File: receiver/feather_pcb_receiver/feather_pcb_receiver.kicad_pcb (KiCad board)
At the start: 2 copper layers, 15 parts, among them J2 uC_Flash, J3 VESC Conn, J4 Utilities Conn, U1 AP2112K-3.3, U2 ATSAMD21G18A-AUT, U3 nRF24L01+, Y1 ABS06-127-32.768KHZ-T‎

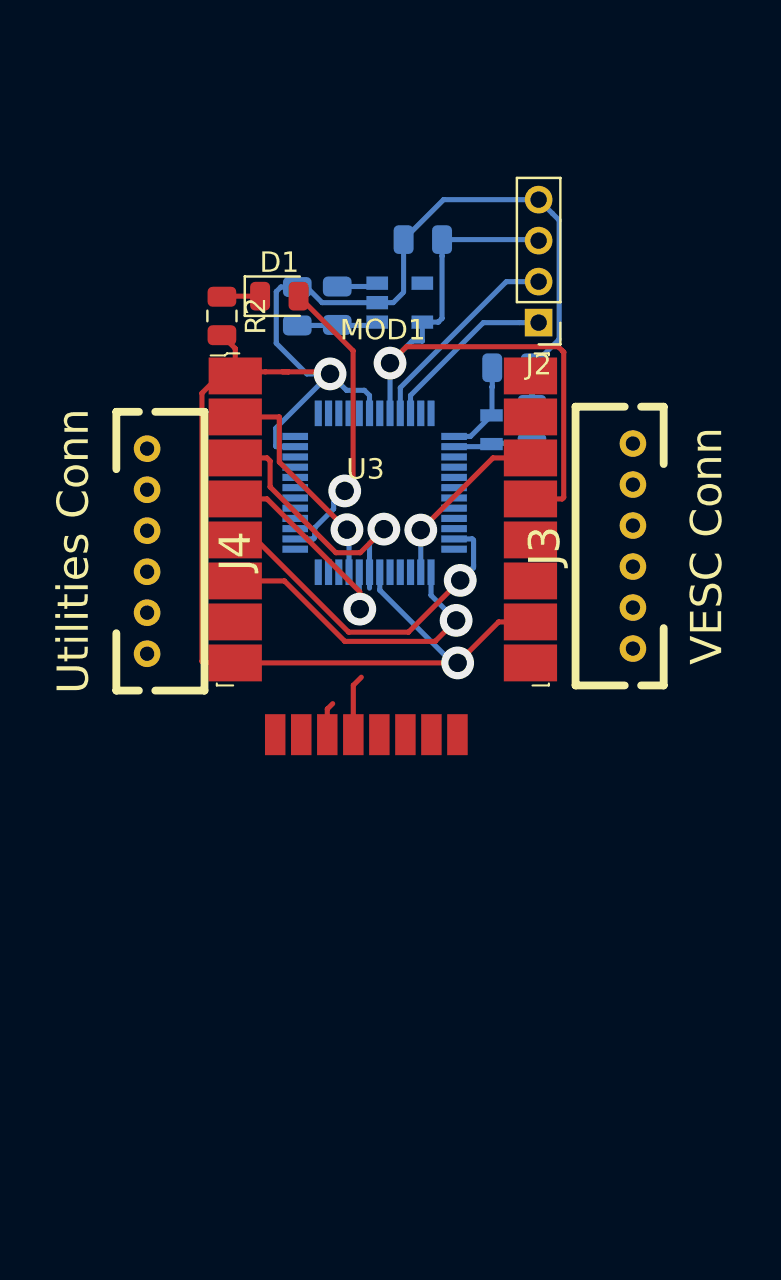
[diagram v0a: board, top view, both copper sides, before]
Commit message: rfm module layout
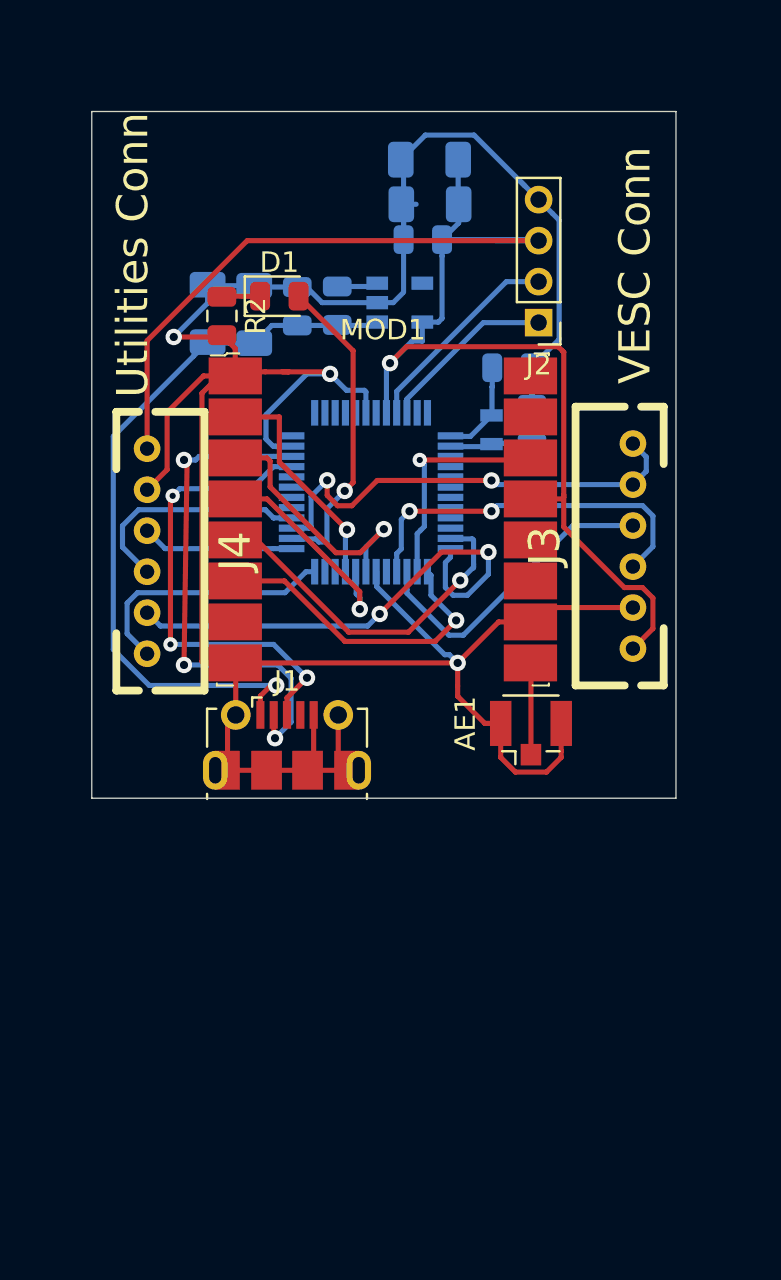
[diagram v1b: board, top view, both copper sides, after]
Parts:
- removed U3: nRF24L01+, mysensors_radios:NRF24L01_PA_LNA-SMD
- added AE1: Antenna_Shield, Connector_Coaxial:U.FL_Hirose_U.FL-R-SMT-1_Vertical, F.Cu at (116.4, 72.3)
- added C1: CP_Small, Capacitor_SMD:C_1206_3216Metric, B.Cu at (102.9, 51.9)
- added C2: 10uF, Capacitor_SMD:C_1206_3216Metric, B.Cu at (100.7, 51.9)
- added C5: 10uF, Capacitor_SMD:C_1206_3216Metric, B.Cu at (111.5, 46.5)
- added C6: CP_Small, Capacitor_SMD:C_1206_3216Metric, B.Cu at (111.5, 44.4)
- added J1: USB_B_Micro, Connector_USB:USB_Micro-B_Molex-105017-0001, F.Cu at (104.5, 72.9)
- moved U2 0.18 mm to (108.6, 60.6)
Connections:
- J3 pad 1: (no net) -> +3V3
- J3 pad 2: (no net) -> GND
- J3 pad 3: (no net) -> VESC1
- J3 pad 4: (no net) -> VESC2
- J3 pad 5: (no net) -> VESC3
- J3 pad 6: (no net) -> VESC3
- J4 pad 1: (no net) -> +3V3
- J4 pad 2: (no net) -> GND
- J4 pad 3: (no net) -> UT1
- J4 pad 4: (no net) -> UT2
- J4 pad 5: (no net) -> UT3
- J4 pad 6: (no net) -> UT4
- MOD1 pad 9: (no net) -> Net-(AE1-Pad1)
- U2 pad 12: (no net) -> UT3
- U2 pad 15: (no net) -> VESC2
- U2 pad 16: (no net) -> VESC1
- U2 pad 22: CSN -> (no net)
- U2 pad 23: CE -> (no net)
- U2 pad 24: (no net) -> UT4
- U2 pad 25: (no net) -> UT1
- U2 pad 27: (no net) -> VESC3
- U2 pad 28: (no net) -> UT2
- U2 pad 33: (no net) -> Net-(J1-Pad3)
- U2 pad 34: (no net) -> Net-(J1-Pad2)
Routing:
- net GND: track 88.1 -> 142.9 mm, vias 2 -> 3
- net +3V3: track 32.8 -> 75.8 mm
- net +5V: track 3.52 -> 35.8 mm, vias 0 -> 1
- net Net-(J1-Pad2): track 0.00 -> 25.3 mm, vias 0 -> 3
- net UT3: track 0.00 -> 24.2 mm, vias 0 -> 2
- net Net-(J1-Pad3): track 0.00 -> 23.2 mm, vias 0 -> 3
- net VESC3: track 0.00 -> 22.6 mm, vias 0 -> 2
- net VESC1: track 0.00 -> 18.3 mm, vias 0 -> 2
- net VESC2: track 0.00 -> 15.1 mm
- net UT4: track 0.00 -> 12.7 mm
- net UT2: track 0.00 -> 11.5 mm
- net UT1: track 0.00 -> 7.41 mm
- net Net-(AE1-Pad1): track 0.00 -> 4.49 mm
- net SCK: track 15.1 -> 12.3 mm
- net Net-(MOD1-Pad14): track 8.86 -> 11.1 mm
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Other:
- board outline added: 28.5 x 33.5 mm
- net class Default: clearance 0.2 -> 0.1; trace_width 0.25 -> 0.1; via_dia 0.8 -> 0.45; via_drill 0.4 -> 0.2
- rule trace_clearance: 0.2 -> 0.1
- rule trace_min: 0.2 -> 0.1
- rule via_min_drill: 0.3 -> 0.2
- rule via_min_size: 0.4 -> 0.45

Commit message: added nrf module
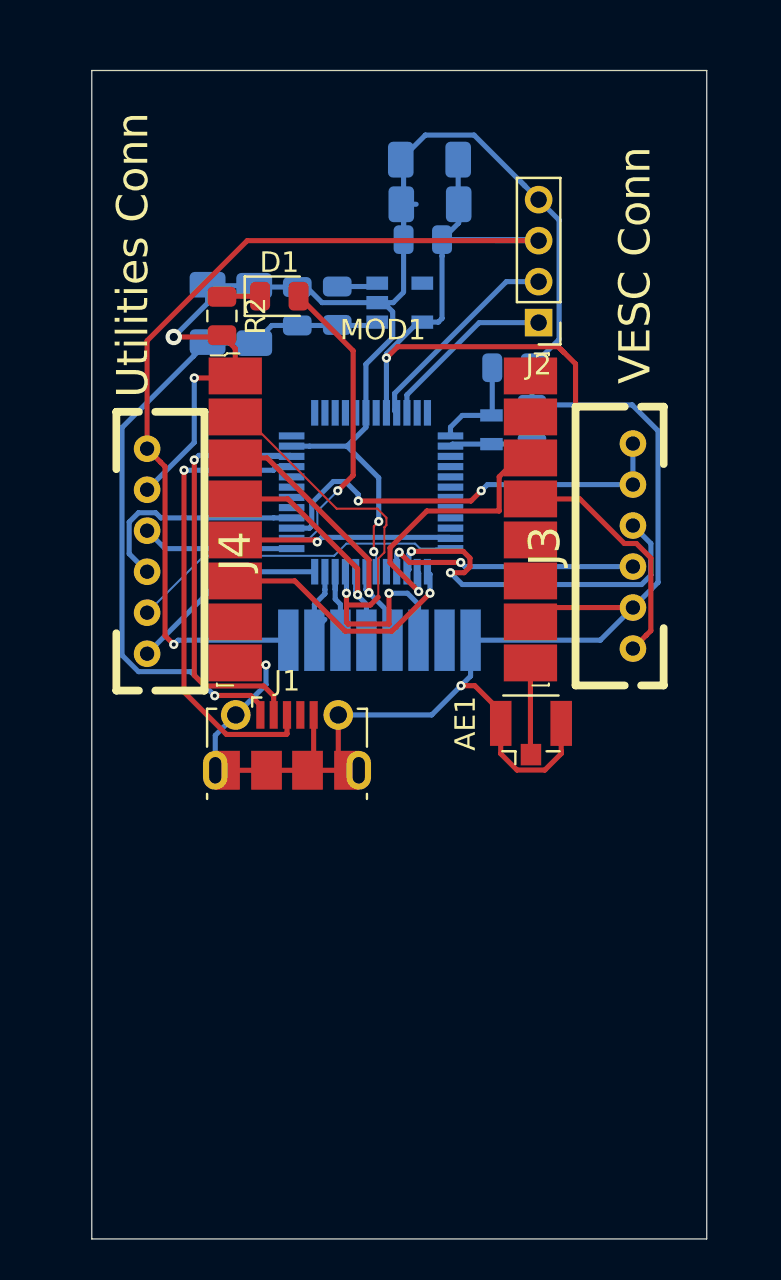
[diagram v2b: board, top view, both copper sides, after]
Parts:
- added U3: YJ13039-NRF24L01, mysensors_radios:YJ-13039-NRF24L01, B.Cu at (103.0, 67.5)
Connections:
- U2 pad 22: (no net) -> CSN
- U2 pad 23: (no net) -> CE
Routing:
- net +3V3: track 75.8 -> 91.9 mm, vias 1 -> 2
- net MISO: track 11.2 -> 25.3 mm, vias 1 -> 2
- net UT3: track 24.2 -> 17.0 mm, vias 2 -> 0
- net Net-(MOD1-Pad5): track 17.3 -> 11.3 mm
- net VESC1: track 18.3 -> 12.7 mm
- net CSN: track 0.00 -> 4.28 mm
- net CE: track 0.00 -> 4.28 mm
- net Net-(J1-Pad2): track 25.3 -> 21.7 mm, vias 3 -> 1
- net VESC2: track 15.1 -> 18.6 mm, vias 0 -> 2
- net Net-(MOD1-Pad6): track 15.4 -> 12.4 mm
- net UT4: track 12.7 -> 9.83 mm
- net +5V: track 35.8 -> 33.5 mm
- net Net-(MOD1-Pad14): track 11.1 -> 13.3 mm
- net VESC3: track 22.6 -> 21.2 mm
- net GND: track 142.9 -> 141.9 mm, vias 3 -> 6
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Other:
- board size 28.5 x 33.5 mm -> 30 x 57 mm
